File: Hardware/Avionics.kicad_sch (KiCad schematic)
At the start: 0 parts

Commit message: Added most parts to schematic and created library part for RP2040
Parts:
- added BT1: 14.8V, symbol Device:Battery_Cell
- added BZ1: 100dB, TerminalBlock_Phoenix:TerminalBlock_Phoenix_MKDS-3-2-5.08_1x02_P5.08mm_Horizontal, symbol Device:Buzzer
- added C? (x2): 27pF, Capacitor_SMD:C_0603_1608Metric_Pad1.08x0.95mm_HandSolder, symbol Device:C_Small
- added C? (x2): 1uF, Capacitor_SMD:C_0603_1608Metric_Pad1.08x0.95mm_HandSolder, symbol Device:C_Small
- added C? (x13): 100nF, Capacitor_SMD:C_0603_1608Metric_Pad1.08x0.95mm_HandSolder, symbol Device:C_Small
- added C? (x3): 10nF, Capacitor_SMD:C_0603_1608Metric_Pad1.08x0.95mm_HandSolder, symbol Device:C_Small
- added C? (x2): 1uF, Capacitor_SMD:C_0402_1005Metric_Pad0.74x0.62mm_HandSolder, symbol Device:C_Small
- added C?: 0.47uF, Capacitor_SMD:C_0603_1608Metric_Pad1.08x0.95mm_HandSolder, symbol Device:C_Small
- added C? (x3): 2.2uF, Capacitor_SMD:C_0603_1608Metric_Pad1.08x0.95mm_HandSolder, symbol Device:C_Small
- added D1: RSX501LAM20, Diode_SMD:D_SOD-128, symbol Device:D_Schottky_Small
- added D2: MBR120, Diode_SMD:D_SOD-123F, symbol Device:D_Schottky_Small
- added D3: PWR, LED_SMD:LED_0603_1608Metric_Pad1.05x0.95mm_HandSolder, symbol Device:LED_Small
- added D4: USB, LED_SMD:LED_0603_1608Metric_Pad1.05x0.95mm_HandSolder, symbol Device:LED_Small
- added D5: FWD, symbol Device:LED_Small
- added D6: BWD, symbol Device:LED_Small
- added D7: PWM, symbol Device:LED_Small
- added D?: WS2812, LED_SMD:LED_WS2812_PLCC6_5.0x5.0mm_P1.6mm, symbol LED:WS2812
- added D? (x4): SS14, symbol Device:D_Schottky_Small
- added J?: USB_C_Receptacle_USB2.0, symbol Connector:USB_C_Receptacle_USB2.0
- added J? (x2): Conn_01x05, symbol Connector_Generic:Conn_01x05
- added J?: SWD, Connector_PinHeader_1.27mm:PinHeader_2x05_P1.27mm_Vertical_SMD, symbol Connector_Generic:Conn_02x05_Odd_Even
- added J?: Micro_SD_Card, symbol Connector:Micro_SD_Card
- added M?: XD-3420, TerminalBlock_Phoenix:TerminalBlock_Phoenix_PT-1,5-2-5.0-H_1x02_P5.00mm_Horizontal, symbol Motor:Motor_DC_ALT
- added Q?: NPN, symbol Device:Q_NPN_BCE
- added Q? (x2): BSS138, Package_TO_SOT_SMD:SOT-23, symbol Transistor_FET:BSS138
- added R1: 5.6KΩ, Resistor_SMD:R_0603_1608Metric_Pad0.98x0.95mm_HandSolder, symbol Device:R_Small_US
- added R10, R? (x5): 10KΩ, Resistor_SMD:R_0603_1608Metric_Pad0.98x0.95mm_HandSolder, symbol Device:R_Small_US
- added R2, R3: 5.1KΩ, Resistor_SMD:R_0603_1608Metric_Pad0.98x0.95mm_HandSolder, symbol Device:R_Small_US
- added R4, R?: R_Small_US, Resistor_SMD:R_0603_1608Metric_Pad0.98x0.95mm_HandSolder, symbol Device:R_Small_US
- added R4, R5: 27Ω, Resistor_SMD:R_0603_1608Metric_Pad0.98x0.95mm_HandSolder, symbol Device:R_Small_US
- added R6: 680Ω, Resistor_SMD:R_0603_1608Metric_Pad0.98x0.95mm_HandSolder, symbol Device:R_Small_US
- added R7, R? (x3): 220Ω, Resistor_SMD:R_0603_1608Metric_Pad0.98x0.95mm_HandSolder, symbol Device:R_Small_US
- added R8, R9: 1KΩ, Resistor_SMD:R_0603_1608Metric_Pad0.98x0.95mm_HandSolder, symbol Device:R_Small_US
- added R?: 100KΩ, Resistor_SMD:R_0603_1608Metric_Pad0.98x0.95mm_HandSolder, symbol Device:R_Small_US
- added R?: 330Ω, Resistor_SMD:R_0603_1608Metric_Pad0.98x0.95mm_HandSolder, symbol Device:R_Small_US
- added SW?: ~{BOOT}, symbol Switch:SW_Push
- added SW?: ~{RESET}, symbol Switch:SW_Push
- added SW?: SW_BATT, symbol Switch:SW_SPST
- added U?: RP2040, RP2040:RP2040-QFN-56, symbol MCU_RaspberryPi:RP2040
- added U?: LP2985-5.0, Package_TO_SOT_SMD:SOT-23-5, symbol Regulator_Linear:LP2985-5.0
- added U?: LP2985-3.3, Package_TO_SOT_SMD:SOT-23-5, symbol Regulator_Linear:LP2985-3.3
- added U?: 74LVC1GU04DRL, Package_TO_SOT_SMD:SOT-553, symbol 74xGxx:74LVC1GU04DRL
- added U?: ICM-20601, Package_LGA:LGA-16_3x3mm_P0.5mm_LayoutBorder3x5y, symbol Sensor_Motion:ICM-20602
- added U?: W25Q128JVS, Package_SO:SOIC-8_5.23x5.23mm_P1.27mm, symbol Memory_Flash:W25Q128JVS
- added U?: L298P, symbol Driver_Motor:L298P
- added Y?: 12MHz, Crystal:Crystal_SMD_7050-4Pin_7.0x5.0mm, symbol Device:Crystal_GND24
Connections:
- new net: C?.2, R9.1, Y?.3
- new net: C?.2, U?.20 (XIN), Y?.1
- new net: R9.2, U?.21 (XOUT)
- new net: J?.4 (Pin_4), U?.24 (SWCLK)
- new net: J?.2 (Pin_2), U?.25 (SWD)
- new net: R5.1, U?.46 (USB_DM)
- new net: R4.1, U?.47 (USB_DP)
- new net: U?.51 (QSPI_SD3), U?.7 (IO3)
- new net: U?.52 (QSPI_SCLK), U?.6 (CLK)
- new net: U?.5 (DI(IO0)), U?.53 (QSPI_SD0)
- new net: U?.3 (IO2), U?.54 (QSPI_SD2)
- new net: U?.2 (DO(IO1)), U?.55 (QSPI_SD1)
- new net: R8.1, U?.1 (~{CS}), U?.56 (QSPI_SS)
- new net: J?.B5 (CC2), R3.1
- new net: C?.1, U?.4 (BP) (x2)
- new net: Q?.1 (B), R?.2
- new net: Q?.3 (D), R?.1, R?.2, U?.15 (IN4), U?.2, U?.7 (IN1)
- new net: D3.1 (K), R6.1
- new net: D1.1 (K), SW?.1 (A)
- new net: BT1.1 (+), D1.2 (A)
- new net: D?.1 (K), D?.2 (A), M?.1 (+), U?.17 (OUT4), U?.4 (OUT1)
- new net: R8.2, SW?.2
- new net: BZ1.2 (+), Q?.2 (C)
- new net: D?.1 (K), D?.2 (A), M?.2 (-), U?.16 (OUT3), U?.5 (OUT2)
- new net: D7.2 (A), R?.2
- new net: Q?.3 (D), R?.1, R?.2, U?.14 (EnB), U?.8 (EnA)
- new net: J?.A5 (CC1), R2.1
- new net: R?.1, U?.13 (IN3), U?.4, U?.9 (IN2)
- new net: C?.1, U?.14 (REGOUT)
- new net: J?.1 (Pin_1), J?.1 (Pin_1)
- new net: J?.2 (Pin_2), J?.2 (Pin_2)
- new net: J?.3 (Pin_3), J?.3 (Pin_3)
- new net: J?.4 (Pin_4), J?.4 (Pin_4)
- new net: J?.5 (Pin_5), J?.5 (Pin_5)
- new net: BZ1.1 (-), R?.2
- new net: D5.2 (A), R?.2
- new net: D4.1 (K), R7.1
- new net: D6.2 (A), R?.2
- new net +1V1: C?.1, C?.1, C?.1, U?.23 (DVDD), U?.45 (VREG_VOUT), U?.50 (DVDD)
- new net +3V3: C?.1, C?.1, C?.1, C?.1, C?.1, C?.1, C?.1, C?.1, C?.1, C?.1, C?.1, C?.1, C?.1, J?.1 (Pin_1), J?.4 (VDD), Q?.1 (G), Q?.1 (G), R10.2, R?.1, R?.1, R?.1, U?.1 (IOVDD), U?.1 (VDDIO), U?.10 (IOVDD), U?.16 (VDD), U?.22 (IOVDD), U?.33 (IOVDD), U?.42 (IOVDD), U?.43 (ADC_AVDD), U?.44 (VREG_IN), U?.48 (USB_VDD), U?.49 (IOVDD), U?.5 (VOUT), U?.8 (VCC)
- new net +5V: C?.1, C?.2, R?.1, R?.1, U?.12 (Vss), U?.5 (VCC), U?.5 (VOUT)
- new net D+: J?.A6 (D+), J?.B6 (D+), R4.2
- new net D-: J?.A7 (D-), J?.B7 (D-), R5.2
- new net DIR: Q?.2 (S), R?.2
- new net GND: BT1.2 (-), C?.1, C?.1, C?.1, C?.2, C?.2, C?.2, C?.2, C?.2, C?.2, C?.2, C?.2, C?.2, C?.2, C?.2, C?.2, C?.2, C?.2, C?.2, C?.2, C?.2, C?.2, C?.2, C?.2, C?.2, C?.2, C?.2, D5.1 (K), D6.1 (K), D7.1 (K), D?.2 (A), D?.2 (A), J?.3 (Pin_3), J?.5 (Pin_5), J?.6 (VSS), J?.7 (Pin_7), J?.9 (Pin_9), J?.9 (SHIELD), J?.A1 (GND), J?.A12 (GND), J?.B1 (GND), J?.B12 (GND), J?.S1 (SHIELD), Q?.3 (E), R2.2, R3.2, R4.2, R6.2, R7.2, R?.2, SW?.1, SW?.1, U?.1 (GND), U?.10 (GND), U?.10 (GND), U?.11 (GND), U?.11 (GND), U?.12 (GND), U?.13 (GND), U?.15 (GND), U?.19 (TESTEN), U?.2 (GND), U?.2 (GND), U?.20 (GND), U?.3 (GND), U?.4 (GND), U?.57 (GND), U?.8 (FSYNC), U?.9 (GND), Y?.2, Y?.4
- new net IMU_CS: U?.16 (GPIO13), U?.5 (~{CS})
- new net IMU_INT: U?.6 (INT)
- new net I_SENSE: R?.1, U?.19 (SENSE_B), U?.2 (SENSE_A)
- new net MISO: J?.7 (DAT0), U?.4 (SAO/SD0)
- new net MOSI: J?.3 (CMD), U?.3 (SDA/SDI)
- new net PWM: Q?.2 (S), R?.2
- new net SCLK: J?.5 (CLK), U?.2 (SCL/SPC)
- new net SPI0_MISO: U?.6 (GPIO4)
- new net SPI0_MOSI: U?.5 (GPIO3)
- new net SPI0_SCLK: U?.4 (GPIO2)
- new net SPI1_MISO: U?.15 (GPIO12)
- new net SPI1_MOSI: U?.14 (GPIO11)
- new net SPI1_SCLK: U?.13 (GPIO10)
- new net USB_DET: R1.2, R4.1, U?.36 (GPIO24)
- new net VBUS: D2.2 (A), D4.2 (A), J?.A4 (VBUS), J?.A9 (VBUS), J?.B4 (VBUS), J?.B9 (VBUS), R1.1
- new net VCC: C?.1, C?.1, C?.1, D2.1 (K), D3.2 (A), D?.1 (K), D?.1 (K), R?.1, SW?.2 (B), U?.1 (VIN), U?.1 (VIN), U?.3 (ON/~{OFF}), U?.3 (ON/~{OFF}), U?.6 (Vs)
- new net ~{RESET}: J?.10 (Pin_10), R10.1, SW?.2, U?.26 (RUN)
- new net ~{SD_CS}: J?.2 (DAT3/CD), R?.2, U?.7 (GPIO5)
- no-connect marks 0 -> 6
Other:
- note added: "Place 1uF caps near 44 and 45"

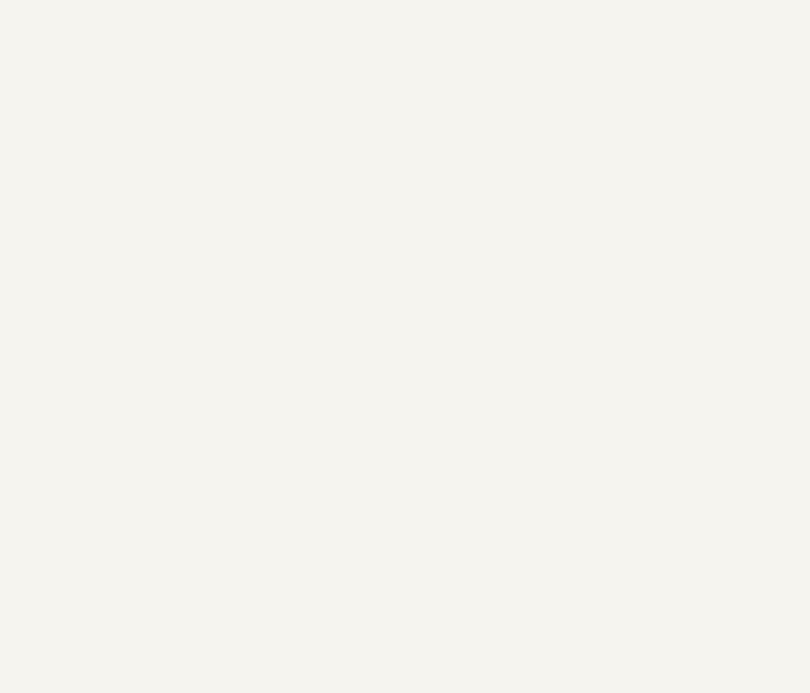
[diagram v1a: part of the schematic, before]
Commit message: Add L298P driver
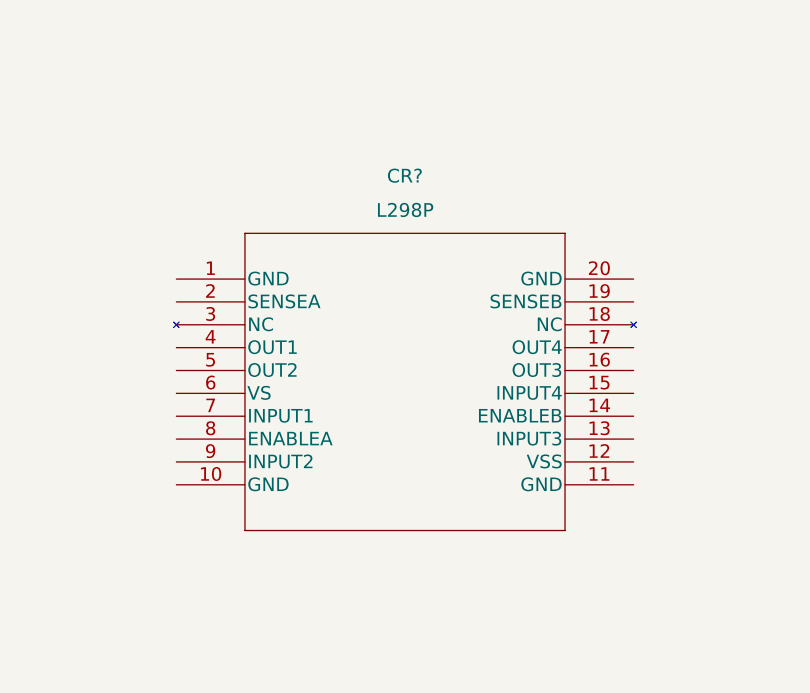
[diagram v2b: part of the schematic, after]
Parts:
- added CR?: L298P, L298P_Dual_Full-Bridge_Driver, symbol L298P:L298P

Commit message: Layout complete, pending review
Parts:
- removed BT1: 14.8V, symbol Device:Battery_Cell
- removed BZ1: 100dB, TerminalBlock_Phoenix:TerminalBlock_Phoenix_MKDS-3-2-5.08_1x02_P5.08mm_Horizontal, symbol Device:Buzzer
- removed C? (x2): 1uF, Capacitor_SMD:C_0603_1608Metric_Pad1.08x0.95mm_HandSolder, symbol Device:C_Small
- removed C? (x2): 10nF, Capacitor_SMD:C_0603_1608Metric_Pad1.08x0.95mm_HandSolder, symbol Device:C_Small
- removed C? (x3): 100nF, Capacitor_SMD:C_0603_1608Metric_Pad1.08x0.95mm_HandSolder, symbol Device:C_Small
- removed C?: 0.47uF, Capacitor_SMD:C_0603_1608Metric_Pad1.08x0.95mm_HandSolder, symbol Device:C_Small
- removed C? (x3): 2.2uF, Capacitor_SMD:C_0603_1608Metric_Pad1.08x0.95mm_HandSolder, symbol Device:C_Small
- removed CR?: L298P, L298P_Dual_Full-Bridge_Driver, symbol L298P:L298P
- removed D2: MBR120, Diode_SMD:D_SOD-123F, symbol Device:D_Schottky_Small
- removed D3: PWR, LED_SMD:LED_0603_1608Metric_Pad1.05x0.95mm_HandSolder, symbol Device:LED_Small
- removed D4: USB, LED_SMD:LED_0603_1608Metric_Pad1.05x0.95mm_HandSolder, symbol Device:LED_Small
- removed D5: FWD, symbol Device:LED_Small
- removed D6: BWD, symbol Device:LED_Small
- removed D7: PWM, symbol Device:LED_Small
- removed D?: WS2812, LED_SMD:LED_WS2812_PLCC6_5.0x5.0mm_P1.6mm, symbol LED:WS2812
- removed D? (x4): SS14, symbol Device:D_Schottky_Small
- removed J? (x2): Conn_01x05, symbol Connector_Generic:Conn_01x05
- removed J?: Micro_SD_Card, symbol Connector:Micro_SD_Card
- removed M?: XD-3420, TerminalBlock_Phoenix:TerminalBlock_Phoenix_PT-1,5-2-5.0-H_1x02_P5.00mm_Horizontal, symbol Motor:Motor_DC_ALT
- removed Q?: NPN, symbol Device:Q_NPN_BCE
- removed Q? (x2): BSS138, Package_TO_SOT_SMD:SOT-23, symbol Transistor_FET:BSS138
- removed R6: 680Ω, Resistor_SMD:R_0603_1608Metric_Pad0.98x0.95mm_HandSolder, symbol Device:R_Small_US
- removed R?: 100KΩ, Resistor_SMD:R_0603_1608Metric_Pad0.98x0.95mm_HandSolder, symbol Device:R_Small_US
- removed R? (x5): 10KΩ, Resistor_SMD:R_0603_1608Metric_Pad0.98x0.95mm_HandSolder, symbol Device:R_Small_US
- removed R?: R_Small_US, Resistor_SMD:R_0603_1608Metric_Pad0.98x0.95mm_HandSolder, symbol Device:R_Small_US
- removed R? (x3): 220Ω, Resistor_SMD:R_0603_1608Metric_Pad0.98x0.95mm_HandSolder, symbol Device:R_Small_US
- removed R?: 330Ω, Resistor_SMD:R_0603_1608Metric_Pad0.98x0.95mm_HandSolder, symbol Device:R_Small_US
- removed SW?: SW_BATT, symbol Switch:SW_SPST
- removed U?: RP2040, RP2040:RP2040-QFN-56, symbol MCU_RaspberryPi:RP2040
- removed U?: LP2985-5.0, Package_TO_SOT_SMD:SOT-23-5, symbol Regulator_Linear:LP2985-5.0
- removed U?: LP2985-3.3, Package_TO_SOT_SMD:SOT-23-5, symbol Regulator_Linear:LP2985-3.3
- removed U?: 74LVC1GU04DRL, Package_TO_SOT_SMD:SOT-553, symbol 74xGxx:74LVC1GU04DRL
- removed U?: ICM-20601, Package_LGA:LGA-16_3x3mm_P0.5mm_LayoutBorder3x5y, symbol Sensor_Motion:ICM-20602
- removed U?: L298P, symbol Driver_Motor:L298P
- removed Y?: 12MHz, Crystal:Crystal_SMD_7050-4Pin_7.0x5.0mm, symbol Device:Crystal_GND24
- added C11, C23: 10uF, Capacitor_SMD:C_0805_2012Metric, symbol Device:C_Small
- added C18, C19, C21, C22: 100nF, Capacitor_SMD:C_0402_1005Metric, symbol Device:C_Small
- added C2: 2.2uF, Capacitor_SMD:C_0603_1608Metric, symbol Device:C_Small
- added C20: 100uF, Capacitor_SMD:CP_Elec_8x6.5, symbol Device:C_Polarized_Small
- added D2: PWR, LED_SMD:LED_0603_1608Metric, symbol Device:LED_Small
- added D3: SK6812BSIDE, SK6812B:SK6812B_Side, symbol LED:SK6812
- added H1, H2, H3, H4: M3, MountingHole:MountingHole_3.2mm_M3_Pad, symbol Mechanical:MountingHole_Pad
- added J3: LiPo 4s, XT60PW-M:AMASS_XT60PW-M, symbol Device:Battery_Cell
- added J4: Qwiic, Connector_JST:JST_SH_BM04B-SRSS-TB_1x04-1MP_P1.00mm_Vertical, symbol Connector_Generic:Conn_01x04
- added J5: PS-562Q, Connector_JST:JST_XH_B2B-XH-A_1x02_P2.50mm_Vertical, symbol Device:Buzzer
- added J6: DM3AT-SF-PEJM5, Connector_Card:microSD_HC_Hirose_DM3AT-SF-PEJM5, symbol Connector:Micro_SD_Card_Det_Hirose_DM3AT
- added J7: XD-3420, TerminalBlock_Phoenix:TerminalBlock_Phoenix_PT-1,5-2-3.5-H_1x02_P3.50mm_Horizontal, symbol Motor:Motor_DC_ALT
- added Q1: BSS138, Package_TO_SOT_SMD:SOT-23, symbol Transistor_FET:BSS138
- added R12, R13: 2.2KΩ, Resistor_SMD:R_0603_1608Metric, symbol Device:R_Small_US
- added R14: 47KΩ, Resistor_SMD:R_0603_1608Metric, symbol Device:R_Small_US
- added R15, R16, R17, R18: 10KΩ, Resistor_SMD:R_0603_1608Metric, symbol Device:R_Small_US
- added R9: 150Ω, Resistor_SMD:R_0603_1608Metric, symbol Device:R_Small_US
- added U2: RP2040, RP2040:RP2040-QFN-56, symbol MCU_RaspberryPi:RP2040
- added U3: NCP1117-3.3, Package_TO_SOT_SMD:SOT-223-3_TabPin2, symbol Regulator_Linear:NCP1117-3.3_SOT223
- added U4: DRV8870DDA, Package_SO:Texas_HTSOP-8-1EP_3.9x4.9mm_P1.27mm_EP2.95x4.9mm_Mask2.4x3.1mm_ThermalVias, symbol Driver_Motor:DRV8870DDA
- added U5: LSM6DSO32, Package_LGA:LGA-14_3x2.5mm_P0.5mm_LayoutBorder3x4y, symbol Sensor_Motion:LSM6DS3
- added Y1: 12MHz, Crystal:Crystal_SMD_Abracon_ABM8G-4Pin_3.2x2.5mm, symbol Device:Crystal_GND24
- C1, C8: renamed from C?; footprint Capacitor_SMD:C_0402_1005Metric_Pad0.74x0.62mm_HandSolder -> Capacitor_SMD:C_0402_1005Metric
- C10, C12, C13, C15, C16, C17, C3, C4, C7, C9: renamed from C?; footprint Capacitor_SMD:C_0603_1608Metric_Pad1.08x0.95mm_HandSolder -> Capacitor_SMD:C_0402_1005Metric
- C14: renamed from C?; value 10nF -> 10uF; footprint Capacitor_SMD:C_0603_1608Metric_Pad1.08x0.95mm_HandSolder -> Capacitor_SMD:C_0805_2012Metric
- C5, C6: renamed from C?; footprint Capacitor_SMD:C_0603_1608Metric_Pad1.08x0.95mm_HandSolder -> Capacitor_SMD:C_0603_1608Metric
- D1: value RSX501LAM20 -> MBR120; footprint Diode_SMD:D_SOD-128 -> Diode_SMD:D_SOD-123F
- J1: renamed from J?; value USB_C_Receptacle_USB2.0 -> DX07S016JA1R1500; footprint (none) -> DX07S016JA1R1500:DX07S016JA1R1500
- R1: renamed from R10; footprint Resistor_SMD:R_0603_1608Metric_Pad0.98x0.95mm_HandSolder -> Resistor_SMD:R_0603_1608Metric
- R10: renamed from R4; footprint Resistor_SMD:R_0603_1608Metric_Pad0.98x0.95mm_HandSolder -> Resistor_SMD:R_0402_1005Metric
- R11: renamed from R5; footprint Resistor_SMD:R_0603_1608Metric_Pad0.98x0.95mm_HandSolder -> Resistor_SMD:R_0402_1005Metric
- R2, R3, R8: footprint Resistor_SMD:R_0603_1608Metric_Pad0.98x0.95mm_HandSolder -> Resistor_SMD:R_0603_1608Metric
- R4: renamed from R1; footprint Resistor_SMD:R_0603_1608Metric_Pad0.98x0.95mm_HandSolder -> Resistor_SMD:R_0603_1608Metric
- R5: renamed from R4; value R_Small_US -> 10KΩ; footprint Resistor_SMD:R_0603_1608Metric_Pad0.98x0.95mm_HandSolder -> Resistor_SMD:R_0603_1608Metric
- R6: renamed from R9; footprint Resistor_SMD:R_0603_1608Metric_Pad0.98x0.95mm_HandSolder -> Resistor_SMD:R_0603_1608Metric
- R7: value 220Ω -> 10KΩ; footprint Resistor_SMD:R_0603_1608Metric_Pad0.98x0.95mm_HandSolder -> Resistor_SMD:R_0603_1608Metric
- SW1, SW2: renamed from SW?; footprint (none) -> Button_Switch_SMD:SW_SPST_B3U-1000P
- gave numbers to parts that had none: 2
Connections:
- net +1V1: now also U2.23 (DVDD), U2.45 (VREG_VOUT), U2.50 (DVDD)
- net +3V3: now also C14.1, R7.1, C18.1, C2.1, C21.1, C22.1, C23.1, D3.2 (VDD), J4.1 (Pin_1), J6.4 (VDD), R12.1, R13.1, R17.1, R18.1, R9.1, U2.1 (IOVDD), U2.10 (IOVDD), U2.22 (IOVDD), U2.33 (IOVDD), U2.42 (IOVDD), U2.43 (ADC_AVDD), U2.44 (VREG_IN), U2.48 (USB_VDD), U2.49 (IOVDD), U3.2 (VO), U4.4 (VREF), U5.12 (CS), U5.5 (VDDIO), U5.8 (VDD)
- net D+: now also R11.1, U2.47 (USB_DP); no longer J1.A6 (D+), J1.B6 (D+), R10.2
- net D-: now also R10.1, U2.46 (USB_DM); no longer J1.A7 (D-), J1.B7 (D-), R11.2
- net GND: now also C11.2, C18.2, C19.2, C2.2, C20.2, C21.2, C22.2, C23.2, D2.1 (K), D3.4 (VSS), H1.1, H2.1, H3.1, H4.1, J3.2 (-), J4.2 (Pin_2), J6.11 (SHIELD), J6.6 (VSS), J6.9 (DET_B), Q1.2 (S), R15.2, R16.2, U2.19 (TESTEN), U2.57 (GND), U3.1 (GND), U4.1 (GND), U4.7 (ISEN), U4.9 (GND), U5.1 (SDO/SA0), U5.2 (SDX), U5.3 (SCX), U5.6 (GND), U5.7 (GND), Y1.2, Y1.4; no longer R7.2
- net IMU_INT: now also U2.12 (GPIO9), U5.4 (INT1)
- net USB_DET: now also U2.3 (GPIO1)
- net VBUS: now also D1.2 (A)
- net VCC: now also D1.1 (K), C11.1, C19.1, C20.1, J3.1 (+), J5.1 (-), R14.1, U3.3 (VI), U4.5 (VM)
- net ~{RESET}: now also U2.26 (RUN)
- net at C6.2: now also U2.21 (XOUT), Y1.3; no longer R6.1
- net at C5.2: now also R6.1, Y1.1
- net at R6.2: now also U2.20 (XIN)
- net at J2.4 (Pin_4): now also U2.24 (SWCLK)
- net at J2.2 (Pin_2): now also U2.25 (SWD)
- net at U1.7 (IO3): now also U2.51 (QSPI_SD3)
- net at U1.6 (CLK): now also U2.52 (QSPI_SCLK)
- net at U1.5 (DI(IO0)): now also U2.53 (QSPI_SD0)
- net at U1.3 (IO2): now also U2.54 (QSPI_SD2)
- net at U1.2 (DO(IO1)): now also U2.55 (QSPI_SD1)
- net at R8.1, U1.1 (~{CS}): now also R7.2, U2.56 (QSPI_SS)
- new net: J7.1 (+), U4.6 (OUT1)
- new net: J7.2 (-), U4.8 (OUT2)
- new net: J5.2 (+), Q1.3 (D)
- new net: D2.2 (A), R9.2
- new net BATT_ADC: R14.2, R15.1, U2.38 (GPIO26_ADC0)
- new net I2C0_SCL: R18.2, U2.16 (GPIO13), U5.13 (SCL)
- new net I2C0_SDA: R17.2, U2.15 (GPIO12), U5.14 (SDA)
- new net I2C1_SCL: J4.4 (Pin_4), R13.2, U2.14 (GPIO11)
- new net I2C1_SDA: J4.3 (Pin_3), R12.2, U2.13 (GPIO10)
- new net MOTOR_PWM1: U2.17 (GPIO14), U4.3 (IN1)
- new net MOTOR_PWM2: U2.18 (GPIO15), U4.2 (IN2)
- new net RGB_DIN: D3.1 (DIN), U2.4 (GPIO2)
- new net SDIO_CLK: J6.5 (CLK), U2.8 (GPIO6)
- new net SDIO_CMD: J6.3 (CMD), U2.9 (GPIO7)
- new net SDIO_DAT0: J6.7 (DAT0), U2.6 (GPIO4)
- new net SDIO_DAT3: J6.2 (DAT3/CD), U2.7 (GPIO5)
- new net SD_DET: J6.10 (DET_A), U2.5 (GPIO3)
- new net SIREN: Q1.1 (G), R16.1, U2.37 (GPIO25)
- new net USB+: J1.A6 (D+), J1.B6 (D+), R11.2
- new net USB-: J1.A7 (D-), J1.B7 (D-), R10.2
- no-connect marks 6 -> 22
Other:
- note added: "Inertial Measurement Unit"
- note added: "LED Indicator"
- note added: "M3 Mounting Holes"
- note added: "Main Power"
- note added: "MicroSD Slot"
- note added: "Microcontroller"
- note added: "Motor Control"
- note added: "Place the 1uF caps across pins 44 and 45"
- note added: "Qwiic Port"
- note added: "Recovery Beacon"
- note added: "USB Type-C"
- note removed: "Place 1uF caps near 44 and 45"
- company: (none) -> MIlwaukee School of Engineering
- title: (none) -> Rocket Avionics - WSGC Collegiate Launch 2022
- moved on the sheet: C1, C10, C12, C13, C14, C15, C16, C17, C3, C4, C5, C6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

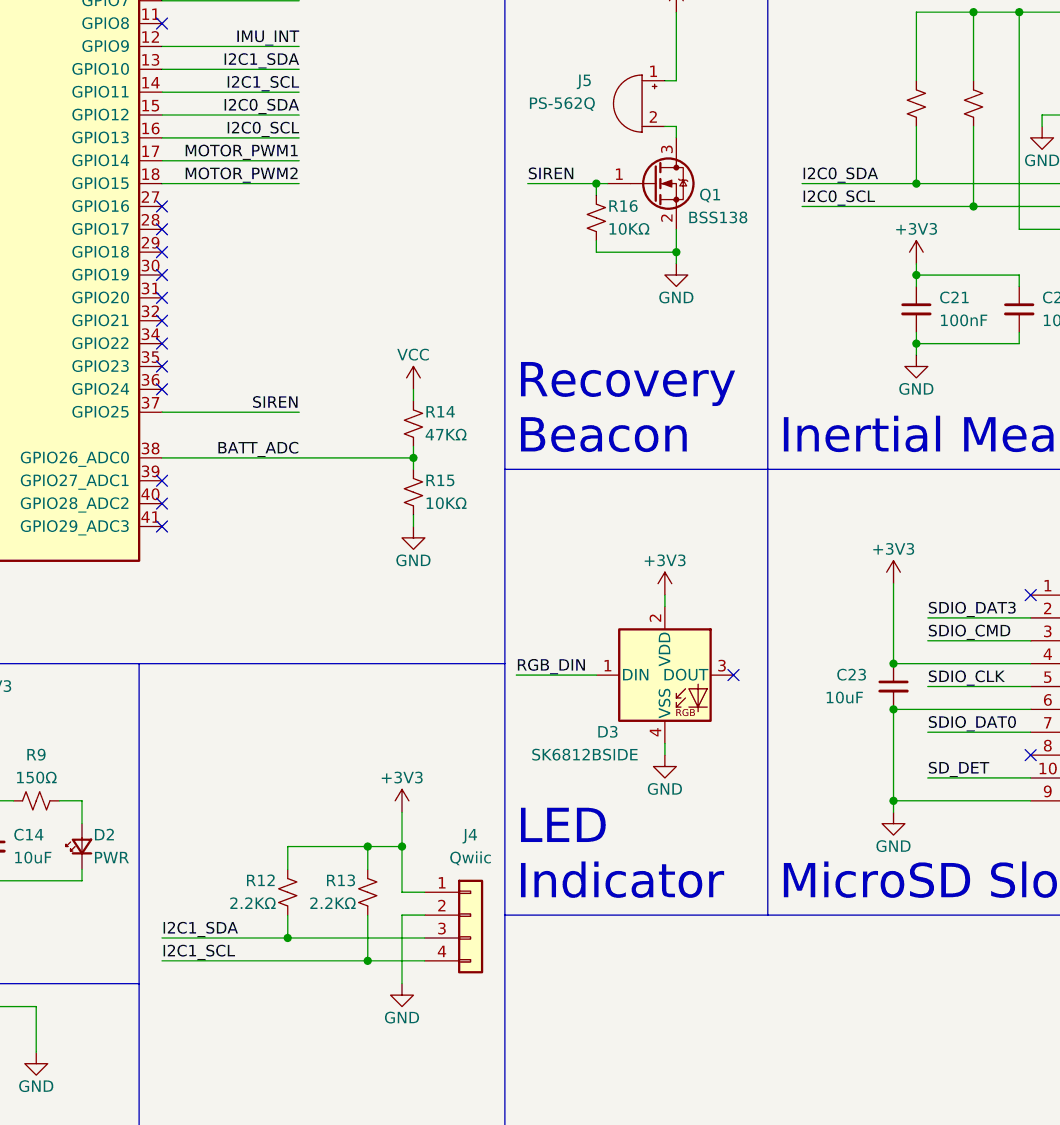
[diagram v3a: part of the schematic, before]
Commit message: Modified layout
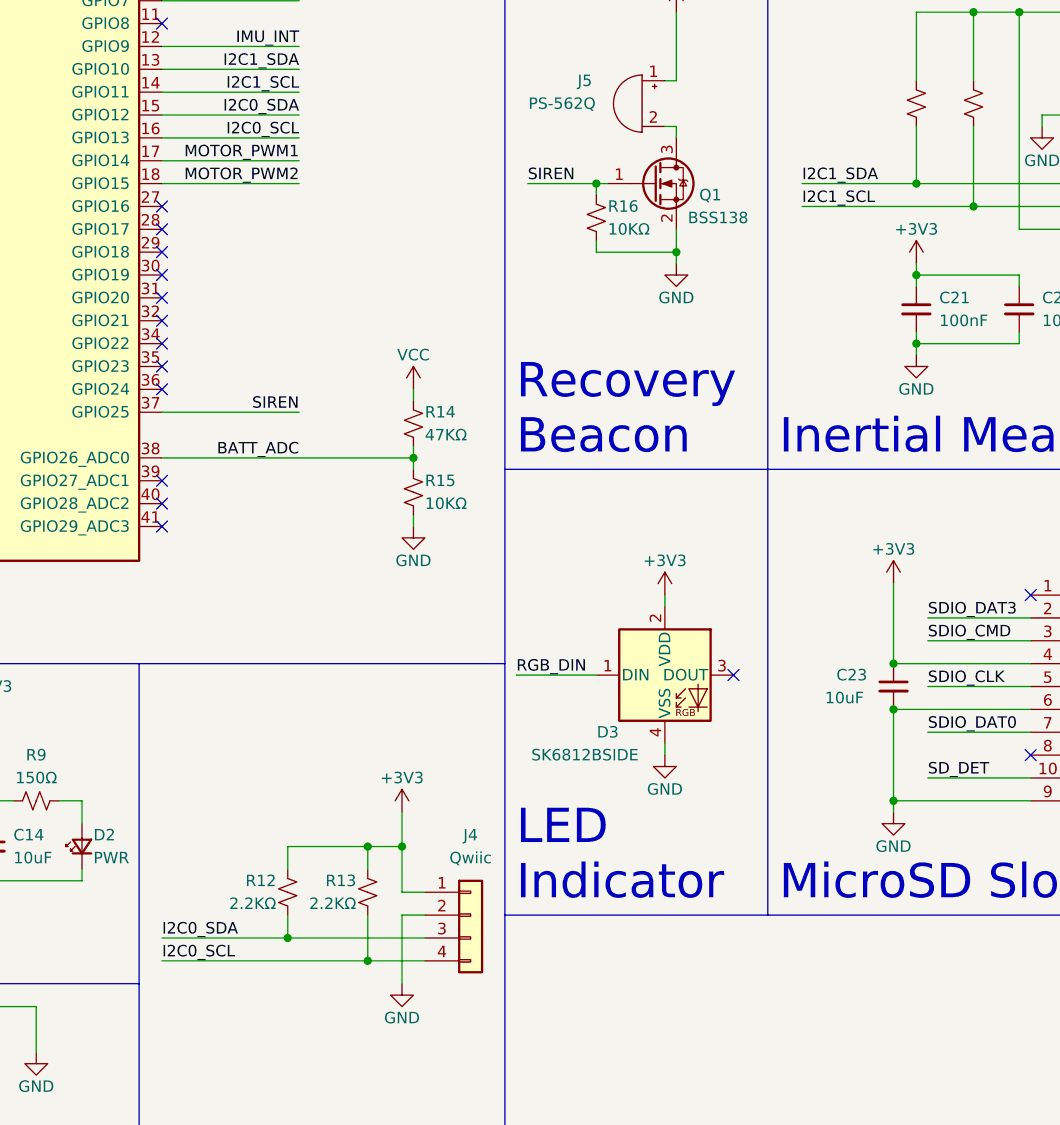
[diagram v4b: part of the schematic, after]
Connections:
- net I2C0_SCL: now also J4.4 (Pin_4), R13.2; no longer R18.2, U5.13 (SCL)
- net I2C0_SDA: now also J4.3 (Pin_3), R12.2; no longer R17.2, U5.14 (SDA)
- net I2C1_SCL: now also R18.2, U5.13 (SCL); no longer J4.4 (Pin_4), R13.2
- net I2C1_SDA: now also R17.2, U5.14 (SDA); no longer J4.3 (Pin_3), R12.2
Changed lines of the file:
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@@
     (effects (font (size 1.27 1.27)) (justify right bottom))
   )
-  (label "I2C1_SDA" (at 120.65 173.99 0)
+  (label "I2C0_SDA" (at 120.65 173.99 0)
     (effects (font (size 1.27 1.27)) (justify left bottom))
   )
-  (label "I2C1_SCL" (at 120.65 176.53 0)
+  (label "I2C0_SCL" (at 120.65 176.53 0)
     (effects (font (size 1.27 1.27)) (justify left bottom))
   )
@@
     (effects (font (size 1.27 1.27)) (justify right bottom))
   )
-  (label "I2C0_SDA" (at 191.77 90.17 0)
-    (effects (font (size 1.27 1.27)) (justify left bottom))
-  )
   (label "MOTOR_PWM1" (at 180.34 40.64 0)
-    (effects (font (size 1.27 1.27)) (justify left bottom))
-  )
-  (label "I2C0_SCL" (at 191.77 92.71 0)
     (effects (font (size 1.27 1.27)) (justify left bottom))
   )
@@
     (effects (font (size 1.27 1.27)) (justify right bottom))
   )
+  (label "I2C1_SDA" (at 191.77 90.17 0)
+    (effects (font (size 1.27 1.27)) (justify left bottom))
+  )
   (label "D+" (at 124.46 46.99 180)
     (effects (font (size 1.27 1.27)) (justify right bottom))
@@
     (effects (font (size 1.27 1.27)) (justify left bottom))
   )
+  (label "I2C1_SCL" (at 191.77 92.71 0)
+    (effects (font (size 1.27 1.27)) (justify left bottom))
+  )
